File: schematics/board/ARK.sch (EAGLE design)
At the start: 164 parts, among them IC1 STM32F103C8T, IC3 MAX809REUR, J2 idc_2x5, Q3 32,768KHz, Q5 8MHz, SW2 RST

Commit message: Новые схемы
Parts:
- removed C43: 100nF, rcl:C-EUC0603
- removed D3, D4: HLMP6, display-hp:HLMP6
- removed IC3: MAX809REUR, MAX809_:MAX809EUR
- removed J2: idc_2x5, idc_2x5:3221-10-0100-00
- removed Q3: 32,768KHz, 9C-8.000MEEJ-T:9C-8.000MEEJ-T
- removed R80, R83: 10k, resistor-shunt:BVS
- removed R84: 10k\, resistor-shunt:BVS
- removed R85, R86: 2k, resistor-shunt:BVS
- removed SJ2: (no value), jumper:SJW
- removed SW2: RST, 1437566-3:1437566-3
- removed U$29, U$36, U$43: FS8205A, CanCubeSat:FS8205A
- added 3,3µH1: 3,3µ, CanCubeSat:B82472G6
- added C005R: 32,768KHz, CanCubeSat:C005R
- added C13, C14, C15, C16: 0,1µ, rcl:C-USC0603
- added C29: 1µ, rcl:C-USC0603
- added C30: 680p, rcl:C-USC1206
- added C31: 4.7µ, rcl:C-USC1206
- added C49: 150µ, CanCubeSat:ECAPECAP150
- added C50: 220µ, CanCubeSat:ECAPECAP220
- added LED1, LED2: (no value), led:LEDCHIPLED_0603
- added R25, R26, R27, R64, R88, R89, R90, R91, R92, R93, R94, R95, R96, R97, R98, R99: 10k, resistor:R-US_R0603
- added R28, R29: 150k, resistor:R-US_R0603
- added R30, R61: ?, resistor:R-US_R0603
- added R31, R58: R01, rcl:R-US_R2512
- added R32, R57, R59, R60: 10R, resistor:R-US_R0603
- added R62: 232k, resistor:R-US_R0603
- added R63: 1M, resistor:R-US_R0603
- added R87: 680k, resistor:R-US_R0603
- added S1: (no value), cansat-lib:UNICS-SWITCH
- added U$16: LTC3119, CanCubeSat:LTC3119
- added U$2, U$9: INA219AID, CanCubeSat:INA219AID
- added U$22: AD5272, CanCubeSat:AD5272
- added U$23: USB-C, CanCubeSat:USB-C
- added U$24, U$25, U$26: FS8205A-, CanCubeSat:FS8205A-
- R78: value 10k -> 1M; device resistor-shunt:BVS -> resistor:R-US_R0603
- R79: value 1M -> 10k; device resistor-shunt:BVS -> resistor:R-US_R0603
- R81, R82: value 10k -> 2k; device resistor-shunt:BVS -> resistor:R-US_R0603
- U$1, U$15, U$8: value FS8205A -> FS8205A-; device CanCubeSat:FS8205A -> CanCubeSat:FS8205A-
- VAR4: device pinheadCS:PINHD-1X6 -> pinheadCS:PINHD-1X8
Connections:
- net PGOOD renamed PGOOD1
- removed net N$153: IC1MCU.PA13, J2.2, R80.2
- removed net N$155: IC1MCU.PA14, J2.4, R81.2
- removed net N$158: J2.10, R84.1, SJ2.1
- removed net N$160: D4.K, R86.1
- removed net N$5: C43.1, IC1MCU.NRST, IC3./RST, R78.2, SJ2.2, SW2.2
- removed net RUN: IC1MCU.PB14, U$59.RUN
- new net BMS1: IC1MCU.PA1, R94.1, R95.1
- new net BMS2: IC1MCU.PA2, R98.1, R99.1
- new net BMS3: IC1MCU.PA3, R92.1, R93.1
- new net BMS4: IC1MCU.PA4, R96.1, R97.1
- new net BMS5: IC1MCU.PA5, R90.1, R91.1
- new net BMS6: IC1MCU.PA6, R88.1, R89.1
- new net BUSPLUS: S1.O, VAR4.7
- new net I2CINT: IC1MCU.PB7, VAR4.3
- new net N$11: 3,3µH1.2, C13.1, U$16.SW1
- new net N$12: 3,3µH1.1, C14.1, U$16.SW2
- new net N$14: C50.1, R31.1, R57.1, R63.2, U$16.PVIN, U$16.VIN
- new net N$17: LED2.C, R81.2
- new net N$26: C31.1, U$16.MPPC, U$16.SVCC, U$16.VCC
- new net N$29: R28.2, U$16.RT
- new net N$31: R30.2, R61.1, U$16.FB
- new net N$32: C13.2, U$16.BST1
- new net N$41: R29.1, U$16.VC
- new net N$42: C30.1, R29.2
- new net N$45: C15.1, R32.2, U$9.IN+
- new net N$47: C15.2, R57.2, U$9.IN-
- new net N$48: C16.1, R59.2, U$2.IN+
- new net N$49: C16.2, R60.2, U$2.IN-
- new net N$50: C49.1, R58.1, R60.1, R61.2, U$16.PVOUT
- new net N$51: C29.1, U$22.CAP
- new net N$52: C14.2, U$16.BST2
- new net N$53: R63.1, U$16.RUN
- new net N$55: R62.2, R87.1, U$59.RUN
- new net PGOOD2: IC1MCU.PB2, U$16.PGOOD
- new net RES-C: IC1MCU.NRST, R79.2, U$23.RES
- new net RX-C: IC1MCU.PA10, U$23.RX+
- new net SWC: IC1MCU.PA14, R27.2, U$23.SWC
- new net SWD: IC1MCU.PA13, R64.2, U$23.SWD
- new net TIME: IC1MCU.PB6, VAR4.2
- new net TX-C: IC1MCU.PA9, U$23.TX+
- net 5V: now also VAR4.8; no longer VAR4.6
- net BMS+: now also R31.2, R32.1; no longer VAR5A.3, VAR5B.3, VAR5C.3
- net BUS+: now also R58.2, R59.1, S1.P; no longer VAR4.5
- net GND: now also C29.2, C30.2, C31.2, C49.2, C50.2, R28.1, R30.1, R62.1, R82.1, U$16.PGND, U$16.PWM, U$16.SGND, U$2.A1, U$2.GND, U$22.A, U$22.GND, U$22.VSS, U$22.W, U$23.GND, U$24.S1, U$25.S1, U$26.S1, U$9.A0, U$9.A1, U$9.GND, VAR5A.4, VAR5B.4, VAR5C.4; no longer C43.2, IC3.GND, J2.3, J2.7, J2.9, R85.1, SW2.1, U$29.S1, U$36.S1, U$43.S1
- net N$104: now also U$1.S2; no longer U$43.S2
- net N$13: now also U$26.S2; no longer U$1.S2
- net N$133: now also R78.1; no longer R79.2
- net N$137: now also R87.2
- net N$145: now also R78.2; no longer R79.1
- net N$148: now also C005R.2; no longer Q3.1
- net N$152: now also C005R.1; no longer Q3.2
- net N$156: now also R25.2; no longer J2.8, R83.2
- net N$157: now also R26.2; no longer J2.6, R82.2
- net N$159: now also LED1.C, R82.2; no longer D3.K, R85.2
- net N$161: now also R81.1; no longer R86.2
- net N$24: now also U$25.S2; no longer U$8.S2
- net N$40: now also U$24.S2; no longer U$15.S2
- net N$72: now also U$15.S2; no longer U$29.S2
- net N$88: now also U$8.S2; no longer U$36.S2
- net OC1: now also R95.2, U$26.G2; no longer U$1.G2
- net OC2: now also R99.2, U$1.G2; no longer U$43.G2
- net OC3: now also R93.2, U$25.G2; no longer U$8.G2
- net OC4: now also R97.2, U$8.G2; no longer U$36.G2
- net OC5: now also R91.2, U$24.G2; no longer U$15.G2
- net OC6: now also R89.2, U$15.G2; no longer U$29.G2
- net OD1: now also R94.2, U$26.G1; no longer U$1.G1
- net OD2: now also R98.2, U$1.G1; no longer U$43.G1
- net OD3: now also R92.2, U$25.G1; no longer U$8.G1
- net OD4: now also R96.2, U$8.G1; no longer U$36.G1
- net OD5: now also R90.2, U$24.G1; no longer U$15.G1
- net OD6: now also R88.2, U$15.G1; no longer U$29.G1
- net RESET: now also U$22.RESET
- net SCL: now also IC1MCU.PB10, U$2.SCL, U$22.SCL, U$9.SCL; no longer IC1MCU.PB6
- net SCLTM: now also IC1MCU.PB8, VAR4.5; no longer IC1MCU.PB10, VAR4.3
- net SDA: now also IC1MCU.PB11, U$2.SDA, U$22.SDA, U$9.SDA; no longer IC1MCU.PB7
- net SDATM: now also IC1MCU.PB9, VAR4.4; no longer IC1MCU.PB11, VAR4.2
- net VDD: now also LED1.A, LED2.A, R25.1, R26.1, R27.1, R64.1, R79.1, U$2.A0, U$2.VCC, U$22.ADDR, U$22.VDD, U$23.VBUS, U$9.VCC, VAR4.6, VAR5A.3, VAR5B.3, VAR5C.3; no longer D3.A, D4.A, IC3.VCC, J2.1, R78.1, R80.1, R81.1, R82.1, R83.1, R84.2, VAR4.4, VAR5A.4, VAR5B.4, VAR5C.4
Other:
- moved on the sheet: C10, C11, C12, C17, C18, C19, C20, C21, C22, C23, C24, C25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

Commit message: изменения схемы АРК
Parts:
- added LED3, LED4, LED5, LED6, LED7, LED8: (no value), led:LEDCHIPLED_0603
- added R100, R80, R83, R84, R85, R86: 1k2, resistor:R-US_R0603
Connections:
- net N$138 renamed 90
- new net N$25: R70.1, U$60.A
- new net N$5: R30.1, U$22.A
- new net N$54: LED3.A, R80.2
- new net N$56: LED4.A, R83.2
- new net N$57: LED5.A, R84.2
- new net N$58: LED6.A, R85.2
- new net N$59: LED7.A, R86.2
- new net N$60: LED8.A, R100.2
- net B-1: now also R86.1
- net B-2: now also R100.1
- net B-3: now also R84.1
- net B-4: now also R85.1
- net B-5: now also R83.1
- net B-6: now also R80.1
- net BUSPLUS: now also LED3.C, LED4.C, LED5.C, LED6.C, LED7.C, LED8.C
- net GND: now also U$22.ADDR; no longer R30.1, R70.1, U$22.A, U$60.A
- net N$26: now also U$22.VDD
- net VDD: no longer U$22.ADDR, U$22.VDD

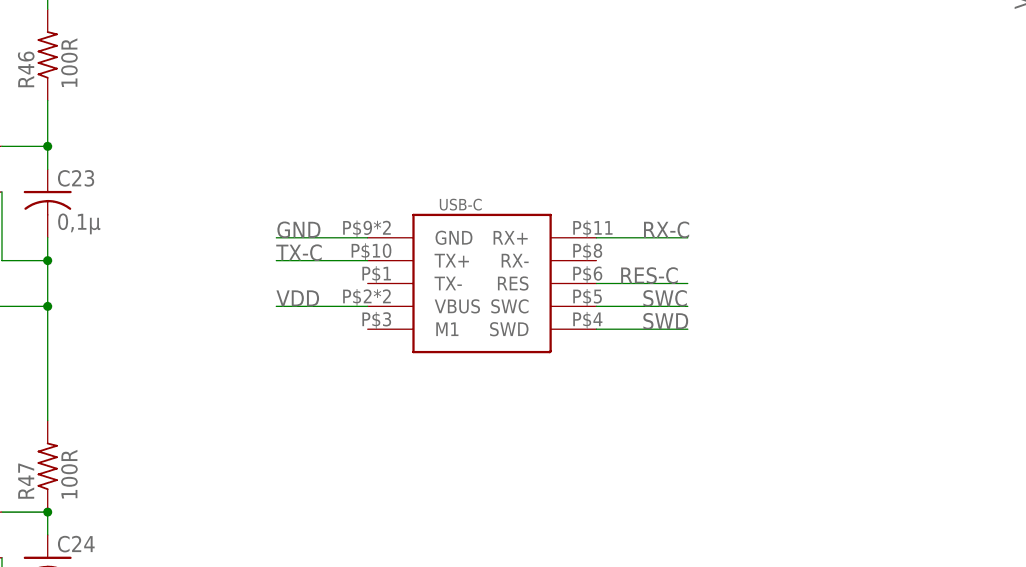
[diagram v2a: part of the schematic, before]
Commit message: доработаны схемы БСК1 и БКУ
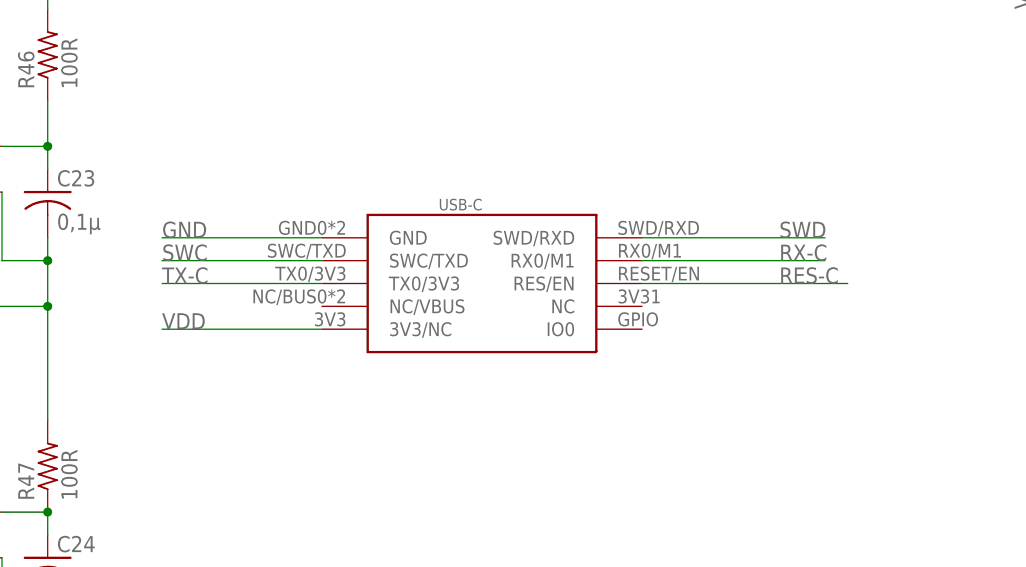
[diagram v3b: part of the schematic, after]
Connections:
- net RES-C: now also U$23.RES/EN; no longer U$23.RES
- net RX-C: now also U$23.RX0/M1; no longer U$23.RX+
- net SWC: now also U$23.SWC/TXD; no longer U$23.SWC
- net SWD: now also U$23.SWD/RXD; no longer U$23.SWD
- net TX-C: now also U$23.TX0/3V3; no longer U$23.TX+
- net VDD: now also U$23.3V3/NC; no longer U$23.VBUS
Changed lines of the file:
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@@
-</segment>
-<segment>
-<pinref part="U$23" gate="G$1" pin="GND"/>
-<wire x1="408.94" y1="220.98" x2="398.78" y2="220.98" width="0.1524" layer="91"/>
-<label x="398.78" y="220.98" size="1.778" layer="95"/>
 </segment>
 <segment>
@@
 <wire x1="208.28" y1="25.4" x2="208.28" y2="43.18" width="0.1524" layer="91"/>
 <label x="208.28" y="35.56" size="1.778" layer="95" rot="R90"/>
+</segment>
+<segment>
+<wire x1="403.86" y1="220.98" x2="386.08" y2="220.98" width="0.1524" layer="91"/>
+<label x="386.08" y="220.98" size="1.778" layer="95"/>
+<pinref part="U$23" gate="G$1" pin="GND"/>
 </segment>
 </net>
@@
 </segment>
 <segment>
-<pinref part="U$23" gate="G$1" pin="VBUS"/>
-<wire x1="408.94" y1="213.36" x2="398.78" y2="213.36" width="0.1524" layer="91"/>
-<label x="398.78" y="213.36" size="1.778" layer="95"/>
-</segment>
-<segment>
 <wire x1="457.2" y1="368.3" x2="447.04" y2="368.3" width="0.1524" layer="91"/>
 <label x="454.66" y="368.3" size="1.778" layer="95" rot="R180"/>
 <pinref part="R79" gate="G$1" pin="1"/>
+</segment>
+<segment>
+<wire x1="403.86" y1="210.82" x2="386.08" y2="210.82" width="0.1524" layer="91"/>
+<label x="386.08" y="210.82" size="1.778" layer="95"/>
+<pinref part="U$23" gate="G$1" pin="3V3/NC"/>
 </segment>
 </net>
@@
 <net name="SWC" class="0">
 <segment>
-<pinref part="U$23" gate="G$1" pin="SWC"/>
-<wire x1="434.34" y1="213.36" x2="444.5" y2="213.36" width="0.1524" layer="91"/>
-<label x="439.42" y="213.36" size="1.778" layer="95"/>
-</segment>
-<segment>
 <wire x1="500.38" y1="266.7" x2="500.38" y2="312.42" width="0.1524" layer="91"/>
 <wire x1="500.38" y1="266.7" x2="495.3" y2="266.7" width="0.1524" layer="91"/>
@@
 <label x="500.38" y="302.26" size="1.778" layer="95" rot="R90"/>
 </segment>
+<segment>
+<label x="386.08" y="218.44" size="1.778" layer="95"/>
+<pinref part="U$23" gate="G$1" pin="SWC/TXD"/>
+<wire x1="386.08" y1="218.44" x2="403.86" y2="218.44" width="0.1524" layer="91"/>
+</segment>
 </net>
 <net name="SWD" class="0">
-<segment>
-<pinref part="U$23" gate="G$1" pin="SWD"/>
-<wire x1="434.34" y1="210.82" x2="444.5" y2="210.82" width="0.1524" layer="91"/>
-<label x="439.42" y="210.82" size="1.778" layer="95"/>
-</segment>
 <segment>
 <wire x1="497.84" y1="259.08" x2="497.84" y2="312.42" width="0.1524" layer="91"/>
@@
 <label x="497.84" y="302.26" size="1.778" layer="95" rot="R90"/>
 </segment>
+<segment>
+<wire x1="439.42" y1="220.98" x2="459.74" y2="220.98" width="0.1524" layer="91"/>
+<label x="454.66" y="220.98" size="1.778" layer="95"/>
+<pinref part="U$23" gate="G$1" pin="SWD/RXD"/>
+</segment>
 </net>
 <net name="TX-C" class="0">
-<segment>
-<pinref part="U$23" gate="G$1" pin="TX+"/>
-<wire x1="408.94" y1="218.44" x2="398.78" y2="218.44" width="0.1524" layer="91"/>
-<label x="398.78" y="218.44" size="1.778" layer="95"/>
-</segment>
 <segment>
 <pinref part="IC1" gate="MCU" pin="PA9"/>
@@
 <label x="487.68" y="302.26" size="1.778" layer="95" rot="R90"/>
 </segment>
+<segment>
+<wire x1="403.86" y1="215.9" x2="386.08" y2="215.9" width="0.1524" layer="91"/>
+<label x="386.08" y="215.9" size="1.778" layer="95"/>
+<pinref part="U$23" gate="G$1" pin="TX0/3V3"/>
+</segment>
 </net>
 <net name="RX-C" class="0">
-<segment>
-<pinref part="U$23" gate="G$1" pin="RX+"/>
-<wire x1="434.34" y1="220.98" x2="444.5" y2="220.98" width="0.1524" layer="91"/>
-<label x="439.42" y="220.98" size="1.778" layer="95"/>
-</segment>
 <segment>
 <pinref part="IC1" gate="MCU" pin="PA10"/>
@@
 <label x="490.22" y="302.26" size="1.778" layer="95" rot="R90"/>
 </segment>
+<segment>
+<wire x1="439.42" y1="218.44" x2="459.74" y2="218.44" width="0.1524" layer="91"/>
+<label x="454.66" y="218.44" size="1.778" layer="95"/>
+<pinref part="U$23" gate="G$1" pin="RX0/M1"/>
+</segment>
 </net>
 <net name="RES-C" class="0">
-<segment>
-<pinref part="U$23" gate="G$1" pin="RES"/>
-<wire x1="434.34" y1="215.9" x2="444.5" y2="215.9" width="0.1524" layer="91"/>
-<label x="436.88" y="215.9" size="1.778" layer="95"/>
-</segment>
 <segment>
 <pinref part="IC1" gate="MCU" pin="NRST"/>
@@
 <label x="467.36" y="375.92" size="1.778" layer="95" rot="R90"/>
 </segment>
-</net>
+<segment>
+<wire x1="439.42" y1="215.9" x2="462.28" y2="215.9" width="0.1524" layer="91"/>
+<label x="454.66" y="215.9" size="1.778" layer="95"/>
+<pinref part="U$23" gate="G$1" pin="RES/EN"/>
+</segment>
+</net>

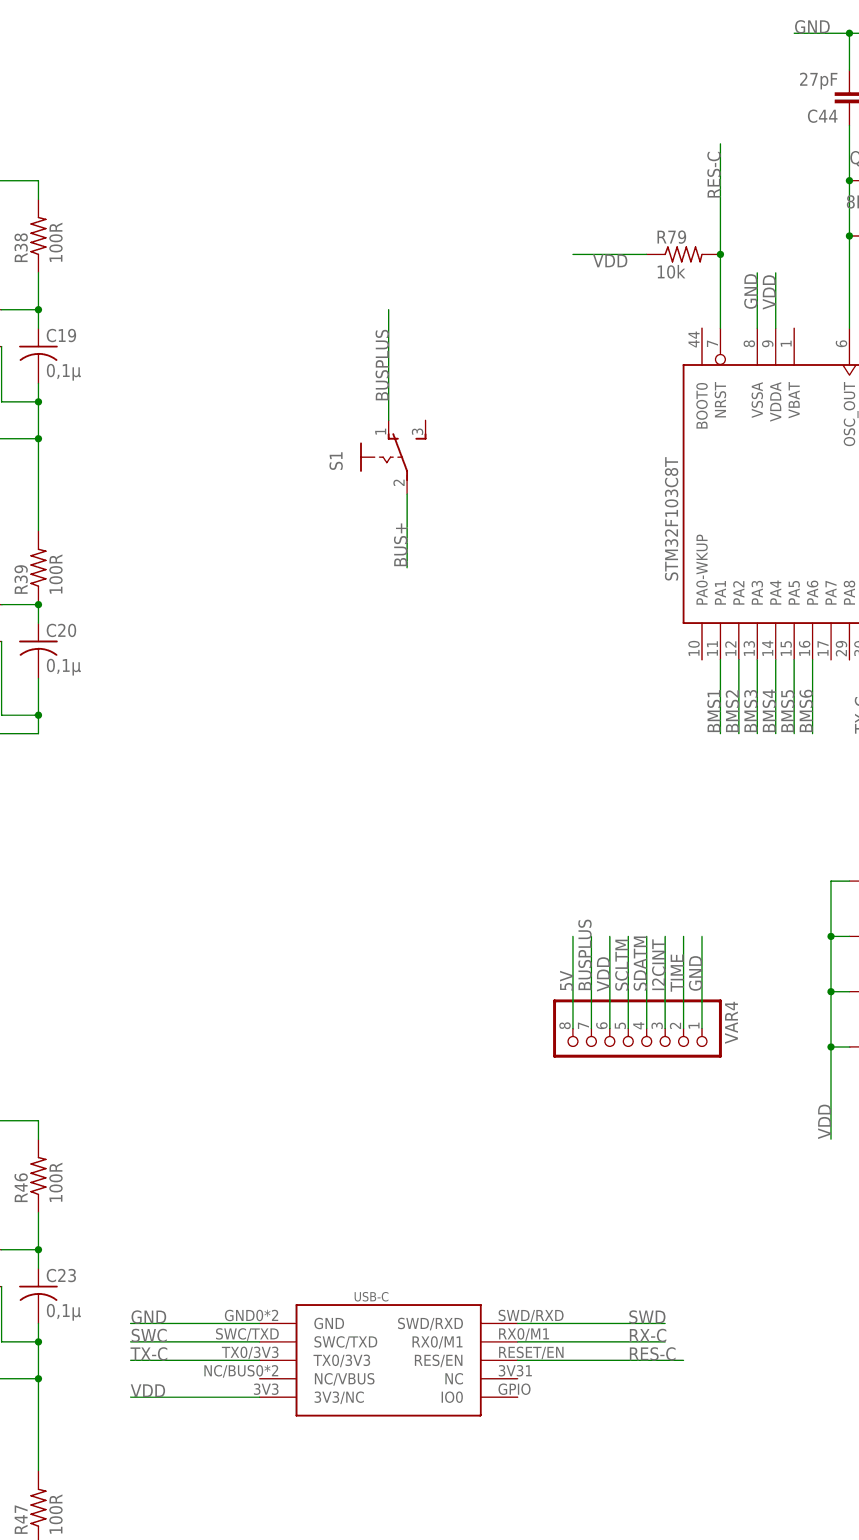
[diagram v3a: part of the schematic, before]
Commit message: обновлена схема БКУ
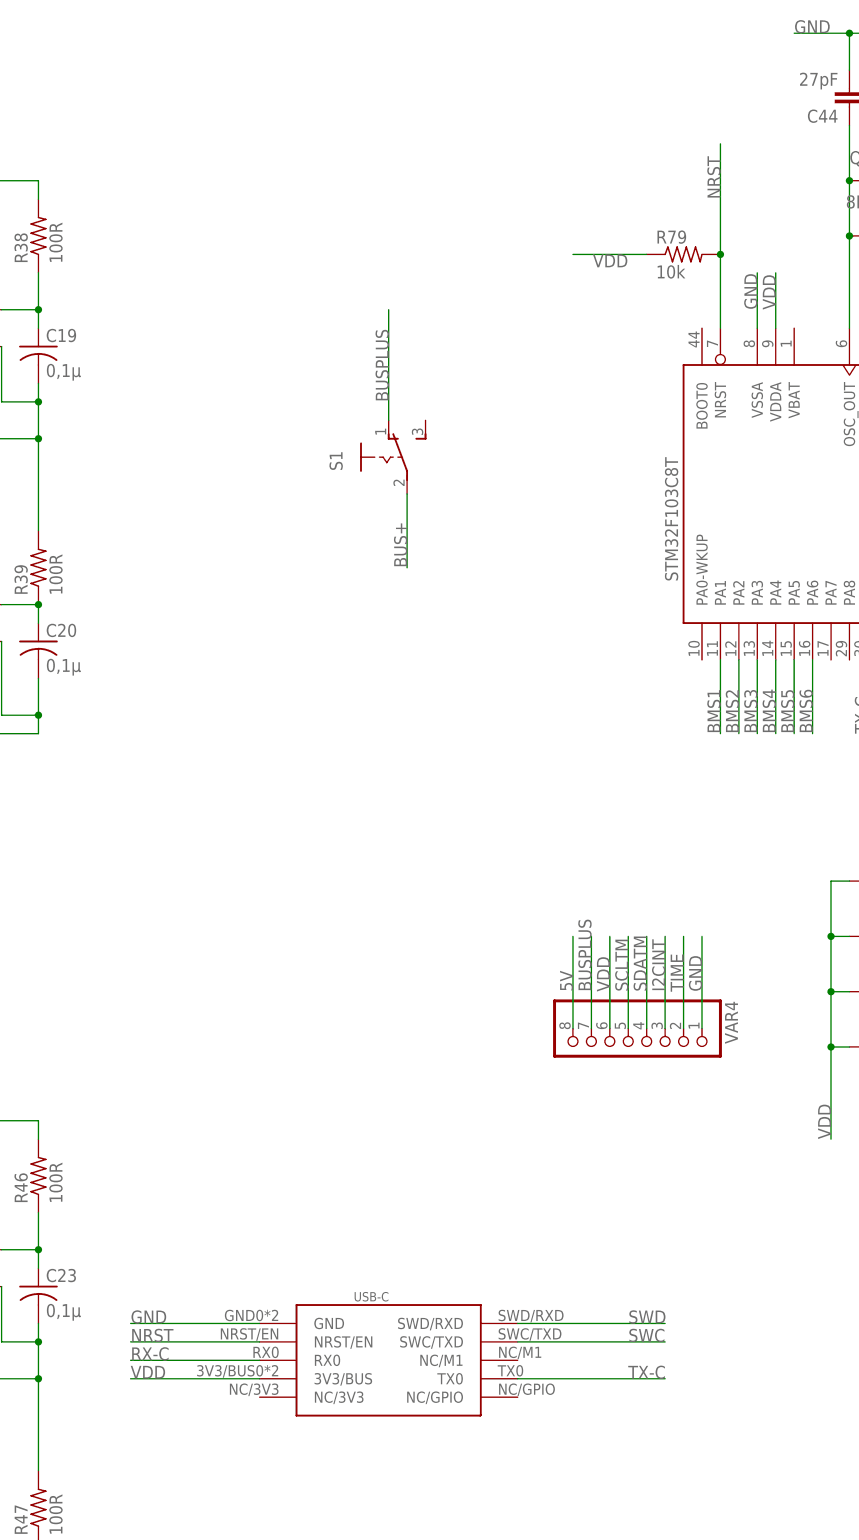
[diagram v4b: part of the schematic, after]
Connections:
- removed net RES-C: IC1MCU.NRST, R79.2, U$23.RES/EN
- new net NRST: IC1MCU.NRST, R79.2, U$23.NRST/EN
- net RX-C: now also U$23.RX0; no longer U$23.RX0/M1
- net TX-C: now also U$23.TX0; no longer U$23.TX0/3V3
- net VDD: now also U$23.3V3/BUS; no longer U$23.3V3/NC
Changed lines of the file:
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@@
 </segment>
 <segment>
-<wire x1="403.86" y1="210.82" x2="386.08" y2="210.82" width="0.1524" layer="91"/>
-<label x="386.08" y="210.82" size="1.778" layer="95"/>
-<pinref part="U$23" gate="G$1" pin="3V3/NC"/>
+<wire x1="403.86" y1="213.36" x2="386.08" y2="213.36" width="0.1524" layer="91"/>
+<label x="386.08" y="213.36" size="1.778" layer="95"/>
+<pinref part="U$23" gate="G$1" pin="3V3/BUS"/>
 </segment>
 </net>
@@
 </segment>
 <segment>
-<label x="386.08" y="218.44" size="1.778" layer="95"/>
+<label x="454.66" y="218.44" size="1.778" layer="95"/>
+<wire x1="439.42" y1="218.44" x2="459.74" y2="218.44" width="0.1524" layer="91"/>
 <pinref part="U$23" gate="G$1" pin="SWC/TXD"/>
-<wire x1="386.08" y1="218.44" x2="403.86" y2="218.44" width="0.1524" layer="91"/>
 </segment>
 </net>
@@
 </segment>
 <segment>
-<wire x1="403.86" y1="215.9" x2="386.08" y2="215.9" width="0.1524" layer="91"/>
-<label x="386.08" y="215.9" size="1.778" layer="95"/>
-<pinref part="U$23" gate="G$1" pin="TX0/3V3"/>
+<wire x1="459.74" y1="213.36" x2="439.42" y2="213.36" width="0.1524" layer="91"/>
+<label x="454.66" y="213.36" size="1.778" layer="95"/>
+<pinref part="U$23" gate="G$1" pin="TX0"/>
 </segment>
 </net>
@@
 </segment>
 <segment>
-<wire x1="439.42" y1="218.44" x2="459.74" y2="218.44" width="0.1524" layer="91"/>
-<label x="454.66" y="218.44" size="1.778" layer="95"/>
-<pinref part="U$23" gate="G$1" pin="RX0/M1"/>
-</segment>
-</net>
-<net name="RES-C" class="0">
+<wire x1="386.08" y1="215.9" x2="403.86" y2="215.9" width="0.1524" layer="91"/>
+<label x="386.08" y="215.9" size="1.778" layer="95"/>
+<pinref part="U$23" gate="G$1" pin="RX0"/>
+</segment>
+</net>
+<net name="NRST" class="0">
 <segment>
 <pinref part="IC1" gate="MCU" pin="NRST"/>
@@
 </segment>
 <segment>
-<wire x1="439.42" y1="215.9" x2="462.28" y2="215.9" width="0.1524" layer="91"/>
-<label x="454.66" y="215.9" size="1.778" layer="95"/>
-<pinref part="U$23" gate="G$1" pin="RES/EN"/>
-</segment>
-</net>
+<wire x1="386.08" y1="218.44" x2="403.86" y2="218.44" width="0.1524" layer="91"/>
+<label x="386.08" y="218.44" size="1.778" layer="95"/>
+<pinref part="U$23" gate="G$1" pin="NRST/EN"/>
+</segment>
+</net>

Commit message: Добавлены светодиоды на платы БСК
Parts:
- added C32, C51: 0,1µ, rcl:C-USC0603
- added C43, C52: 10µ, rcl:C-USC1206
- C30, C36, C38: device rcl:C-USC1206 -> rcl:C-USC0603
- R30: value ? -> 150k
- R61: value ? -> 680k
- R70: value 51k -> 150k
- R83: value 1k2 -> 2k
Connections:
- removed net N$26: C31.1, U$16.MPPC, U$16.SVCC, U$16.VCC, U$22.VDD
- removed net RESET: IC1MCU.PB15, U$22.RESET, U$60.RESET
- new net DPC_RST: IC1MCU.PB14, U$60.RESET
- new net DPD_RST: IC1MCU.PB15, U$22.RESET
- net BUSPLUS: no longer LED4.C
- net GND: now also C32.2, C43.2, C51.2, C52.2
- net N$25: now also C32.1, C43.1, U$60.VDD
- net N$5: now also C51.1, C52.1, U$22.VDD
- net VDD: now also C31.1, LED4.C, U$16.MPPC, U$16.SVCC, U$16.VCC; no longer U$60.VDD
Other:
- moved on the sheet: LED2, R81
